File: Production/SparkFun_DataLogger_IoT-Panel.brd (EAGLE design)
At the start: 115.8 x 161.3 mm, 816 parts, among them J10 QWIIC_RIGHT_ANGLE, J12 MICRO-SD-PUSH-PUSH-EXT-PIN, J13 Vertical Qwiic Connector, J17 QWIIC_RIGHT_ANGLE, J21 MICRO-SD-PUSH-PUSH-EXT-PIN, J22 Vertical Qwiic Connector, J26 QWIIC_RIGHT_ANGLE, J3 MICRO-SD-PUSH-PUSH-EXT-PIN, J30 MICRO-SD-PUSH-PUSH-EXT-PIN, J31 Vertical Qwiic Connector, J35 QWIIC_RIGHT_ANGLE, J39 MICRO-SD-PUSH-PUSH-EXT-PIN, J4 Vertical Qwiic Connector, J40 Vertical Qwiic Connector, J44 QWIIC_RIGHT_ANGLE, J48 MICRO-SD-PUSH-PUSH-EXT-PIN, J49 Vertical Qwiic Connector, J53 QWIIC_RIGHT_ANGLE, U1 ESP-WROOM-32E, U10 74HC4066_QUAD_BILATERAL_SWITC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, U11 CH340C, U12 XC6222B331MR-G, U13 MAX17048, U14 MCP73831, U15 XC6222B331MR-G, U16 74HC4066_QUAD_BILATERAL_SWITC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, U17 74HC4066_QUAD_BILATERAL_SWITC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, U18 ESP-WROOM-32E, U19 CH340C, U2 CH340C, U20 XC6222B331MR-G, U21 MAX17048, U22 MCP73831, U23 XC6222B331MR-G, U24 74HC4066_QUAD_BILATERAL_SWITC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, U25 74HC4066_QUAD_BILATERAL_SWITC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, U26 ESP-WROOM-32E, U27 CH340C, U28 XC6222B331MR-G, U29 MAX17048, U3 XC6222B331MR-G, U30 MCP73831, U31 XC6222B331MR-G, U32 74HC4066_QUAD_BILATERAL_SWITC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, U33 74HC4066_QUAD_BILATERAL_SWITC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, U34 ESP-WROOM-32E, U35 CH340C, U36 XC6222B331MR-G, U37 MAX17048, U38 MCP73831, U39 XC6222B331MR-G, U4 MAX17048, U40 74HC4066_QUAD_BILATERAL_SWITC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, U41 74HC4066_QUAD_BILATERAL_SWITC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, U42 ESP-WROOM-32E, U43 CH340C, U44 XC6222B331MR-G, U45 MAX17048, U46 MCP73831, U47 XC6222B331MR-G, U48 74HC4066_QUAD_BILATERAL_SWITC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, U5 MCP73831, U6 XC6222B331MR-G, U7 74HC4066_QUAD_BILATERAL_SWITC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, U8 ESP-WROOM-32E, U9 74HC4066_QUAD_BILATERAL_SWITC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

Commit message: Post design review updates.
Change BO silk for D5.
Remove unused PURs.
Clean up wire stubs.
Remove GND guard trace.
Add GND vias near switching vias.
Renumber Schematic.
Repanelize and pull together outer border.
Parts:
- removed PWREN, PWREN1, VIN, VIN1: TEST-POINT3X5, SparkFun-Connectors:PAD.03X.05
- added TP13, TP17, TP21, TP9: TEST-POINT3X5, SparkFun-Connectors:PAD.03X.05
- C10, C14, C23, C27, C5: value 2.2uF -> 0.1uF
- C12: value 2.2uF -> 10nF
- C13, C15, C17, C19, C31: value 0.1uF -> 2.2uF
- C4: value 10nF -> 2.2uF
- D1: value BLUE -> 3A/10V/280mV; device SparkFun-LED:LED-0603 -> SparkFun-DiscreteSemi:SOD-323
- D2: value B3DQ3BRG -> 3A/10V/280mV; device RA_RGB:B3DQ3BRG -> SparkFun-DiscreteSemi:SOD-323
- D3: value Yellow -> 3A/10V/280mV; device SparkFun-LED:LED-0603 -> SparkFun-DiscreteSemi:SOD-323
- D4: value 3A/10V/280mV -> TVS; device SparkFun-DiscreteSemi:SOD-323 -> SparkFun-DiscreteSemi:0603
- D5: value 3A/10V/280mV -> Yellow; device SparkFun-DiscreteSemi:SOD-323 -> SparkFun-LED:LED-0603
- D6: value 3A/10V/280mV -> B3DQ3BRG; device SparkFun-DiscreteSemi:SOD-323 -> RA_RGB:B3DQ3BRG
- D7: value TVS -> BLUE; device SparkFun-DiscreteSemi:0603 -> SparkFun-LED:LED-0603
- J1: value (none) -> MICRO-SD-PUSH-PUSH-EXT-PIN; device SparkFun-Connectors:USB-C-16P_4LAYER-PADS -> SparkFun-Connectors:MICROSD-EXTERNALPIN
- J10: value QWIIC_RIGHT_ANGLE -> (none); device SparkFun-Connectors:JST04_1MM_RA -> SparkFun-Connectors:USB-C-16P_4LAYER-PADS
- J2: device SparkFun-Connectors:JST-2-SMD -> SparkFun-Connectors:1X06_NO_SILK
- J3: value MICRO-SD-PUSH-PUSH-EXT-PIN -> QWIIC_RIGHT_ANGLE; device SparkFun-Connectors:MICROSD-EXTERNALPIN -> SparkFun-Connectors:JST04_1MM_RA
- J4: value Vertical Qwiic Connector -> (none); device SparkFun-Connectors:JST04_1MM_VERT -> SparkFun-Connectors:USB-C-16P_4LAYER-PADS
- J6: value (none) -> Vertical Qwiic Connector; device SparkFun-Connectors:1X04_NO_SILK -> SparkFun-Connectors:JST04_1MM_VERT
- J7: device SparkFun-Connectors:1X06_NO_SILK -> SparkFun-Connectors:1X09_NO_SILK
- J8: device SparkFun-Connectors:1X09_NO_SILK -> SparkFun-Connectors:1X04_NO_SILK
- J9: device SparkFun-Connectors:USB-C-16P_4LAYER-PADS -> SparkFun-Connectors:JST-2-SMD
- LOGO1: value QWIIC_LOGO_6MM -> SFE_LOGO_NAME.2_INCH; device SparkFun-Aesthetics:QWIIC_6MM -> SparkFun-Aesthetics:SFE_LOGO_NAME_.2
- LOGO2: value OSHW-LOGOS -> SFE_LOGO_FLAME.2_INCH; device SparkFun-Aesthetics:OSHW-LOGO-S -> SparkFun-Aesthetics:SFE_LOGO_FLAME_.2
- LOGO4: value OSHW-LOGOS -> QWIIC_LOGO_6MM; device SparkFun-Aesthetics:OSHW-LOGO-S -> SparkFun-Aesthetics:QWIIC_6MM
- LOGO5: value SFE_LOGO_NAME.2_INCH -> OSHW-LOGOS; device SparkFun-Aesthetics:SFE_LOGO_NAME_.2 -> SparkFun-Aesthetics:OSHW-LOGO-S
- LOGO6: value SFE_LOGO_FLAME.2_INCH -> OSHW-LOGOS; device SparkFun-Aesthetics:SFE_LOGO_FLAME_.2 -> SparkFun-Aesthetics:OSHW-LOGO-S
- R1, R2: value 5.1k -> 10k
- R13: value 10k -> 1k
- R14: value 10k -> 2.0K
- R15: value 10k -> 2.2k
- R16: value 2.2k -> 100k
- R17: value 100k -> 9.1K; device SparkFun-Resistors:0402-TIGHT -> RA_RGB:0402-TIGHT
- R18: value 5.1k -> 2.2k
- R20: value 10k -> 5.1k
- R6: value 2.2k -> 10k
- R7: value 2.0K -> 10k
- R8: value 1k -> 5.1k
- R9: value 9.1K -> 5.1k; device RA_RGB:0402-TIGHT -> SparkFun-Resistors:0402-TIGHT
- U$12, U$120, U$160, U$200, U$240, U$80: device output:#5_#_D5#0 -> output:#5#0
- U10: value 74HC4066_QUAD_BILATERAL_SWITCH_QFN -> ESP-WROOM-32E; device SparkFun-IC-Logic:14-QFN -> SparkFun-RF:ESP-WROOM-32D-NARROW
- U2: value CH340C -> 74HC4066_QUAD_BILATERAL_SWITCH_QFN; device SparkFun-IC-Comms:SO016 -> SparkFun-IC-Logic:14-QFN
- U4: value MAX17048 -> CH340C; device SparkFun-IC-Power:DFN-8 -> SparkFun-IC-Comms:SO016
- U6: value XC6222B331MR-G -> 74HC4066_QUAD_BILATERAL_SWITCH_QFN; device SparkFun-IC-Power:SOT23-5 -> SparkFun-IC-Logic:14-QFN
- U7: value 74HC4066_QUAD_BILATERAL_SWITCH_QFN -> MAX17048; device SparkFun-IC-Logic:14-QFN -> SparkFun-IC-Power:DFN-8
- U8: value ESP-WROOM-32E -> XC6222B331MR-G; device SparkFun-RF:ESP-WROOM-32D-NARROW -> SparkFun-IC-Power:SOT23-5
- moved TP5 103.5 mm to (88.1, 2.54)
- moved C29 91.7 mm to (97.8, 21.6), turned to 90 degrees
- moved TP4 82.0 mm to (12.7, 15.2), turned to 0 degrees
- moved TP2 81.8 mm to (8.89, 22.9), turned to 0 degrees
- moved TP6 80.9 mm to (64.0, 15.2), turned to 0 degrees
- moved R22 79.0 mm to (85.6, 13.8), turned to 0 degrees
- moved LOGO1 75.4 mm to (25.4, 31.8), flipped to the bottom
- moved J9 71.6 mm to (5.08, 6.99), turned to 180 degrees
- moved U7 59.1 mm to (4.95, 15.9), turned to 0 degrees
- moved C23 57.2 mm to (3.05, 15.9), turned to 90 degrees
- moved FD1 57.2 mm to (49.8, 3.30), flipped to the top
- moved FD2 57.2 mm to (49.8, 3.30), flipped to the bottom
- moved FD3 57.2 mm to (2.54, 35.6)
- moved FD4 57.2 mm to (2.54, 35.6)
- moved J5 53.4 mm to (1.27, 29.2)
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- renumbered PWREN2 to TP10, PWREN3 to TP14, PWREN4 to TP18, PWREN5 to TP22, VIN10 to TP23, VIN11 to TP24, VIN2 to TP7, VIN3 to TP8, VIN4 to TP11, VIN5 to TP12, VIN6 to TP15, VIN7 to TP16, VIN8 to TP19, VIN9 to TP20
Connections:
- net !RESET!: now also C5.1, J7.9, R1.1, U2.12; no longer C31.1, J8.9, R3.1, U9.12
- net !RESET!1: now also U10.3, U9.12; no longer U7.12, U8.3
- net 3.3V: now also C11.1, C12.1, C13.1, C17.1, C18.1, C6.1, C7.1, J2.5, R1.2, R10.2, R16.1, U2.14, U3.5, U4.16, U4.4, U6.14; no longer C1.1, C15.1, C2.1, C25.1, C26.1, C27.1, C28.1, J7.5, R17.1, R22.2, R3.2, U10.14, U2.16, U2.4, U6.5, U9.14
- net 3.3V1: now also C28.1, U10.2, U9.14; no longer C21.1, U7.14, U8.2
- net 3.3V_SW: now also C1.1, C2.1, C25.1, C26.1, C27.1, C8.1, D6.2, J1.4, J3.2, J6.2, J8.2, R2.2, R3.2, R4.2, R5.2, R6.2, U8.5; no longer C18.1, C19.1, C20.1, C5.1, C6.1, C7.1, D2.2, J10.2, J3.4, J4.2, J5.2, R10.2, R11.2, R12.2, R13.2, R14.2, U3.5
- net 3.3V_SW1: now also R22.2; no longer R20.2
- net 5V: now also D3.A, J2.3; no longer D6.A, J7.3
- net CH340-DTR: now also R11.2, U4.13; no longer R4.2, U2.13
- net CH340-RTS: now also R12.2, U4.14; no longer R5.2, U2.14
- net CH340-RX: now also U4.3; no longer U2.3
- net CH340-RX1: now also U10.35; no longer U8.35
- net CH340-TX: now also U4.2; no longer U2.2
- net CH340-TX1: now also U10.34; no longer U8.34
- net D+: now also J4.A6, J4.B6, U4.5; no longer J1.A6, J1.B6, U2.5
- net D+1: now also J10.A6, J10.B6; no longer J9.A6, J9.B6
- net D-: now also J4.A7, J4.B7, U4.6; no longer J1.A7, J1.B7, U2.6
- net D-1: now also J10.A7, J10.B7; no longer J9.A7, J9.B7
- net ESP0/!BOOT!: now also J7.8; no longer J8.8
- net ESP0/!BOOT!1: now also U10.25; no longer U8.25
- net ESP1: now also U10.9; no longer U8.9
- net ESP12/DAT1: now also U10.14, U9.4; no longer U7.4, U8.14
- net ESP12/DAT2: now also U2.4; no longer U9.4
- net ESP13/DAT1: now also U10.16; no longer U8.16
- net ESP13/DAT3: now also J1.2, R2.1; no longer J3.2, R14.1
- net ESP14/CLK: now also J1.5; no longer J3.5
- net ESP14/CLK1: now also U10.13; no longer U8.13
- net ESP15/CMD: now also U2.8; no longer U9.8
- net ESP15/CMD1: now also U10.23, U9.8; no longer U7.8, U8.23
- net ESP16/RXD: now also J7.3; no longer J8.3
- net ESP16/RXD1: now also U10.27; no longer U8.27
- net ESP17/TXD: now also J7.4; no longer J8.4
- net ESP17/TXD1: now also U10.28; no longer U8.28
- net ESP18/SCK: now also J5.4; no longer J6.4
- net ESP18/SCK1: now also U10.30; no longer U8.30
- net ESP19/POCI: now also J5.2, R10.1; no longer J6.2, R22.1
- net ESP19/POCI1: now also U10.31; no longer U8.31
- net ESP2: now also U10.29; no longer U8.29
- net ESP2/DAT0: now also U2.1; no longer U9.1
- net ESP2/DAT1: now also U10.24, U9.1; no longer U7.1, U8.24
- net ESP21/SDA: now also R15.1, U6.4, U7.8; no longer R19.1, U10.4, U4.8
- net ESP21/SDA1: now also U10.33; no longer U8.33
- net ESP22/SCL: now also R18.2, U6.11, U7.7; no longer R16.2, U10.11, U4.7
- net ESP22/SCL1: now also U10.36; no longer U8.36
- net ESP23/PICO: now also J5.3; no longer J6.3
- net ESP23/PICO1: now also U10.37; no longer U8.37
- net ESP25/LED: now also J7.2, R19.2; no longer J8.2, R6.2
- net ESP25/LED1: now also U10.10; no longer U8.10
- net ESP26/RGBLED: now also J7.1; no longer J8.1
- net ESP26/RGBLED1: now also U10.11; no longer U8.11
- net ESP32/PWREN: now also U2.11; no longer U9.11
- net ESP32/PWREN1: now also U10.8, U9.11; no longer U7.11, U8.8
- net ESP33: now also J5.1; no longer J6.1
- net ESP35/A1: now also U10.7; no longer U8.7
- net ESP35/A7: now also R16.2, R17.1; no longer R17.2, R9.1
- net ESP36/A0: now also J7.7; no longer J8.7
- net ESP36/A1: now also U10.4; no longer U8.4
- net ESP39/A1: now also U10.5; no longer U8.5
- net ESP39/A3: now also J7.6; no longer J8.6
- net ESP4/DAT1: now also J1.8, R4.1; no longer J3.8, R12.1
- net ESP4/DAT2: now also U10.26; no longer U8.26
- net ESP5: now also J7.5; no longer J8.5
- net GND: now also C21.2, C22.2, C23.2, C24.2, D4.1, D6.1, D7.C, J1.10, J1.11, J1.12, J1.13, J1.6, J2.2, J2.4, J2.6, J3.1, J4.GND, J4.GND2, J6.1, J8.1, J9.1, R14.1, R17.2, R8.1, R9.1, U2.7, U2.EPAD, U6.13, U6.6, U6.7, U6.EPAD, U7.1, U7.4, U7.6, U7.9, U8.2; no longer C28.2, C29.2, C30.2, C31.2, D1.C, D2.1, D7.1, J1.GND, J1.GND2, J10.1, J2.1, J3.10, J3.11, J3.12, J3.13, J3.6, J4.1, J5.1, J7.2, J7.4, J7.6, R1.1, R15.1, R2.1, R9.2, U10.13, U10.6, U10.7, U10.EPAD, U2.1, U4.4, U4.6, U4.9, U6.2, U9.7, U9.EPAD
- net GND1: now also C28.2, C29.2, C30.2, C31.2, J10.GND, J10.GND2, R20.1, U10.1, U10.15, U10.38, U10.GND1, U10.GNDT1, U10.GNDT2, U10.GNDT3, U10.GNDT4, U10.GNDT5, U10.GNDT6, U10.GNDT7, U10.GNDT8, U9.7, U9.EPAD; no longer C21.2, C22.2, C23.2, C24.2, J9.GND, J9.GND2, R18.1, U7.7, U7.EPAD, U8.1, U8.15, U8.38, U8.GND1, U8.GNDT1, U8.GNDT2, U8.GNDT3, U8.GNDT4, U8.GNDT5, U8.GNDT6, U8.GNDT7, U8.GNDT8
- net N$1: now also J4.B5, R8.2; no longer J1.B5, R1.2
- net N$10: now also R13.2, TP3.1; no longer R8.2, VIN1.1
- net N$11: now also R14.2; no longer R7.2
- net N$12: now also D6.3; no longer D2.3
- net N$13: now also D7.A; no longer D1.A
- net N$14: now also J10.B5, R20.2; no longer J9.B5, R18.2
- net N$15: now also J10.A5; no longer J9.A5
- net N$16: now also R18.1; no longer R16.1
- net N$17: now also R15.2; no longer R19.2
- net N$2: now also J4.A5, R9.2; no longer J1.A5, R2.2
- net N$20: now also TP5.1; no longer TP2.1
- net N$3: now also D1.C, D2.C, D3.C; no longer D4.C, D5.C, D6.C
- net N$35: now also TP9.1; no longer TP3.1
- net N$4: now also R12.1; no longer R5.1
- net N$5: now also R11.1; no longer R4.1
- net N$50: now also TP13.1; no longer TP4.1
- net N$6: now also R19.1; no longer R6.1
- net N$65: now also TP17.1; no longer TP5.1
- net N$7: now also D6.4; no longer D2.4
- net N$8: now also D5.A; no longer D3.A
- net N$80: now also TP21.1; no longer TP6.1
- net N$9: now also D5.C, R13.1; no longer D3.C, R8.1
- net PWREN: now also R7.2, TP4.1, U2.10, U2.13, U2.5, U2.6, U6.12, U6.5, U8.3; no longer PWREN.1, R15.2, U10.12, U10.5, U3.3, U9.10, U9.13, U9.5, U9.6
- net PWREN1: now also TP6.1, U9.10, U9.13, U9.5, U9.6; no longer PWREN1.1, U7.10, U7.13, U7.5, U7.6
- net QWIIC_SCL: now also J3.4, J6.4, J8.4, U6.10; no longer J10.4, J4.4, J5.4, U10.10
- net QWIIC_SDA: now also J3.3, J6.3, J8.3, U6.3; no longer J10.3, J4.3, J5.3, U10.3
- net SD_CMD: now also J1.3, R6.1, U2.9; no longer J3.3, R10.1, U9.9
- net SD_CMD1: now also R21.1, U9.9; no longer R20.1, U7.9
- net SD_DAT0: now also J1.7, R5.1, U2.2; no longer J3.7, R11.1, U9.2
- net SD_DAT1: now also R22.1, U9.2; no longer R21.1, U7.2
- net SD_DAT2: now also J1.1, R3.1, U2.3; no longer J3.1, R13.1, U9.3
- net SD_DAT3: now also U9.3; no longer U7.3
- net SHIELD: now also J4.SHLD1, J4.SHLD2, J4.SHLD3, J4.SHLD4; no longer J1.SHLD1, J1.SHLD2, J1.SHLD3, J1.SHLD4
- net SHIELD1: now also J10.SHLD1, J10.SHLD2, J10.SHLD3, J10.SHLD4; no longer J9.SHLD1, J9.SHLD2, J9.SHLD3, J9.SHLD4
- net VIN: now also C15.1, C19.1, C21.1, C22.1, C24.1, TP2.1, U3.3, U8.1; no longer C12.1, C16.1, C17.1, C29.1, C8.1, U6.1, U6.3, VIN.1
- net VIN1: now also C29.1, C31.1; no longer C22.1, C24.1
- net V_BATT: now also C16.1, C20.1, C23.1, D1.A, J2.1, J9.2, U7.2, U7.3; no longer C11.1, C13.1, C30.1, D4.A, J2.2, J7.1, U4.2, U4.3
- net V_BATT1: now also C30.1; no longer C23.1
- net V_USB: now also D2.A, D4.2, J4.VBUS1, J4.VBUS2; no longer D5.A, D7.2, J1.VBUS1, J1.VBUS2
- net V_USB1: now also J10.VBUS1, J10.VBUS2; no longer J9.VBUS1, J9.VBUS2
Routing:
- net GND3: track 45.3 -> 21.1 mm, vias 101 -> 104
- net GND5: track 45.3 -> 21.1 mm, vias 101 -> 104
- net GND2: track 45.3 -> 21.1 mm, vias 101 -> 104
- net GND: track 45.3 -> 21.1 mm, vias 101 -> 104
- net GND4: track 45.3 -> 21.1 mm, vias 101 -> 104
- net GND1: track 45.3 -> 21.1 mm, vias 101 -> 104
- net ESP18/SCK2: track 49.0 -> 42.5 mm, vias 2 -> 1
- net ESP18/SCK4: track 49.0 -> 42.5 mm, vias 2 -> 1
- net ESP18/SCK3: track 49.0 -> 42.5 mm, vias 2 -> 1
- net ESP18/SCK: track 49.0 -> 42.5 mm, vias 2 -> 1
- net ESP18/SCK1: track 49.0 -> 42.5 mm, vias 2 -> 1
- net ESP18/SCK5: track 49.0 -> 42.5 mm, vias 2 -> 1
- net ESP23/PICO: track 36.9 -> 34.0 mm
- net ESP23/PICO4: track 36.9 -> 34.0 mm
- net ESP23/PICO2: track 36.9 -> 34.0 mm
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- added copper zone on layer 15, net 3.3V_SW
- added copper zone on layer 15, net 3.3V_SW1
- added copper zone on layer 15, net 3.3V_SW2
- added copper zone on layer 15, net 3.3V_SW3
- added copper zone on layer 15, net 3.3V_SW4
- added copper zone on layer 15, net 3.3V_SW5
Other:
- outline, holes or cut-outs redrawn

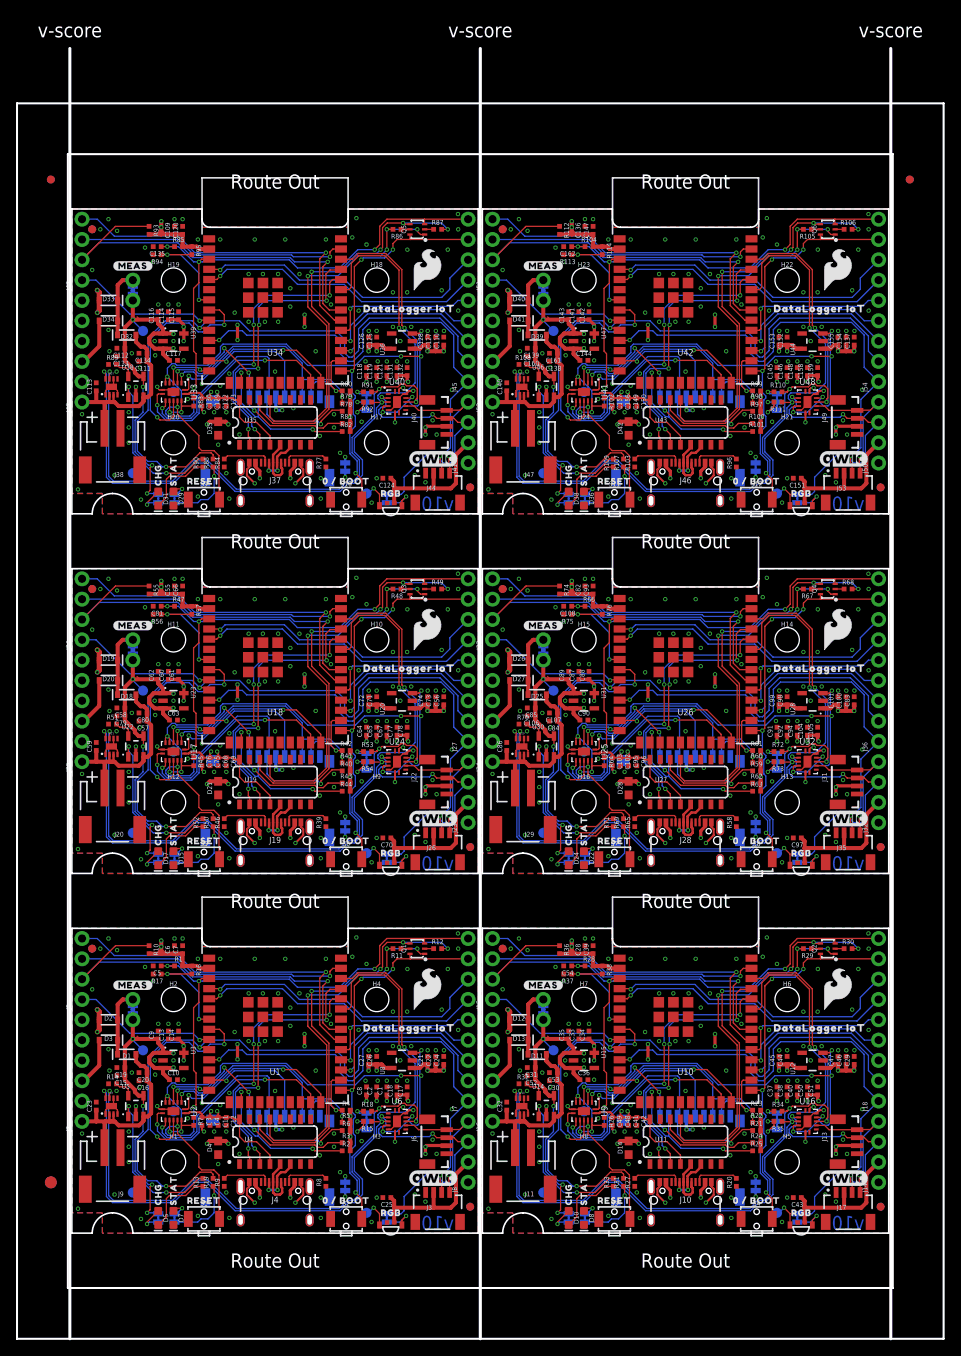
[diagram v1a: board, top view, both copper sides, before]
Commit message: Update for v11 PCB
Removed OSHW logo.
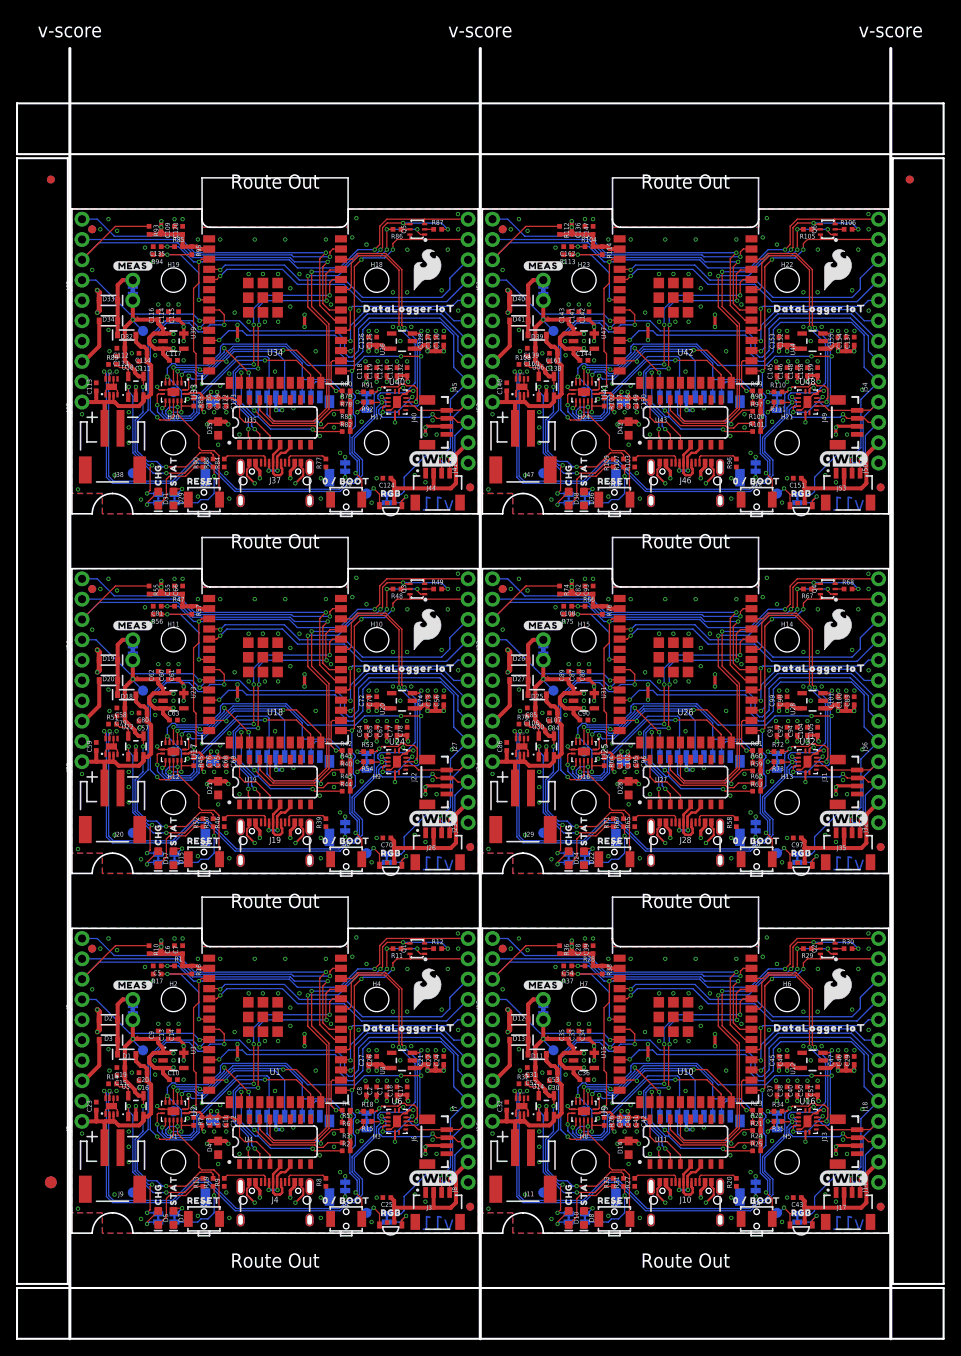
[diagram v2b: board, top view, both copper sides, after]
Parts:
- removed LOGO19, LOGO23: SFE_LOGO_NAME.2_INCH, SparkFun-Aesthetics:SFE_LOGO_NAME_.2
- removed LOGO20, LOGO24: SFE_LOGO_FLAME.2_INCH, SparkFun-Aesthetics:SFE_LOGO_FLAME_.2
- removed LOGO21: QWIIC_LOGO_6MM, SparkFun-Aesthetics:QWIIC_6MM
- removed LOGO22: OSHW-LOGOS, SparkFun-Aesthetics:OSHW-LOGO-S
- LOGO10: value OSHW-LOGOS -> QWIIC_LOGO_6MM; device SparkFun-Aesthetics:OSHW-LOGO-S -> SparkFun-Aesthetics:QWIIC_6MM
- LOGO14, LOGO5: value OSHW-LOGOS -> SFE_LOGO_NAME.2_INCH; device SparkFun-Aesthetics:OSHW-LOGO-S -> SparkFun-Aesthetics:SFE_LOGO_NAME_.2
- LOGO15: value SFE_LOGO_NAME.2_INCH -> SFE_LOGO_FLAME.2_INCH; device SparkFun-Aesthetics:SFE_LOGO_NAME_.2 -> SparkFun-Aesthetics:SFE_LOGO_FLAME_.2
- LOGO16: value SFE_LOGO_FLAME.2_INCH -> QWIIC_LOGO_6MM; device SparkFun-Aesthetics:SFE_LOGO_FLAME_.2 -> SparkFun-Aesthetics:QWIIC_6MM
- LOGO17: value QWIIC_LOGO_6MM -> SFE_LOGO_NAME.2_INCH; device SparkFun-Aesthetics:QWIIC_6MM -> SparkFun-Aesthetics:SFE_LOGO_NAME_.2
- LOGO18, LOGO6: value OSHW-LOGOS -> SFE_LOGO_FLAME.2_INCH; device SparkFun-Aesthetics:OSHW-LOGO-S -> SparkFun-Aesthetics:SFE_LOGO_FLAME_.2
- LOGO7: value SFE_LOGO_NAME.2_INCH -> QWIIC_LOGO_6MM; device SparkFun-Aesthetics:SFE_LOGO_NAME_.2 -> SparkFun-Aesthetics:QWIIC_6MM
- LOGO8: value SFE_LOGO_FLAME.2_INCH -> SFE_LOGO_NAME.2_INCH; device SparkFun-Aesthetics:SFE_LOGO_FLAME_.2 -> SparkFun-Aesthetics:SFE_LOGO_NAME_.2
- LOGO9: value QWIIC_LOGO_6MM -> SFE_LOGO_FLAME.2_INCH; device SparkFun-Aesthetics:QWIIC_6MM -> SparkFun-Aesthetics:SFE_LOGO_FLAME_.2
- moved LOGO8 84.2 mm to (25.4, 76.7), flipped to the bottom
- moved LOGO14 78.1 mm to (25.4, 121.7)
- moved LOGO10 72.0 mm to (96.5, 51.8), flipped to the top
- moved LOGO18 71.5 mm to (95.8, 120.4), flipped to the top
- moved LOGO13 68.2 mm to (45.2, 96.8)
- moved LOGO15 54.3 mm to (44.5, 120.4), flipped to the top
- moved LOGO5 53.2 mm to (76.7, 31.8)
- moved LOGO11 51.3 mm to (76.7, 76.7)
- moved LOGO12 51.3 mm to (95.8, 75.4)
- moved LOGO17 40.1 mm to (76.7, 121.7), flipped to the bottom
- moved LOGO7 37.3 mm to (45.2, 51.8), flipped to the top
- moved LOGO9 23.6 mm to (44.5, 75.4)
- moved LOGO6 22.9 mm to (95.8, 30.5), flipped to the top
- moved LOGO16 21.3 mm to (96.5, 96.8)
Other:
- outline, holes or cut-outs redrawn
- board text added: "v11"
- board text removed: "v10"
